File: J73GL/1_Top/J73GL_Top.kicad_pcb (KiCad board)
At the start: 2 copper layers, 315.8 x 99.2 mm, 90 parts, among them J10 Conn_01x01, J11 Conn_01x01, J12 Conn_01x01, J13 Conn_01x01, J14 Conn_01x01, J15 Conn_01x01, J16 Conn_01x01, J17 Conn_01x01, J2 Conn_01x01, J3 Conn_01x01, J4 Conn_01x01, J5 Conn_01x01, J6 Conn_01x01, J7 Conn_01x01, J8 Conn_01x01, J9 Conn_01x01, SW1 SW_PUSH, SW2 KEY_SWITCH, SW3 SW_PUSH, SW4 KEY_SWITCH, SW4 SW_PUSH, SW5 SW_PUSH, SW7 SW_PUSH, SW8 SW_PUSH

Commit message: 色々更新
・J74GLからJ73GLに変更
・色々進捗
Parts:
- removed the SW8 at (295.3, 85.7)
- SW4: footprint kbd:SW_Hole_2u -> kbd:SW_Hole_2.25u
- SW8: footprint kbd:SW_Hole -> kbd:SW_Hole_1.75
- moved SW8 11.9 mm to (288.1, 85.7)
- moved SW8 4.76 mm to (223.8, 85.7)
- moved SW8 4.76 mm to (185.7, 85.7)
- moved SW8 4.76 mm to (128.6, 85.7)
- moved SW8 4.76 mm to (90.5, 85.7)
- moved SW8 4.76 mm to (71.4, 85.7)
- moved SW8 4.76 mm to (242.9, 85.7)
- moved SW8 4.76 mm to (261.9, 85.7)
- moved SW8 4.76 mm to (204.8, 85.7)
- moved SW8 4.76 mm to (147.6, 85.7)
- moved SW8 4.76 mm to (166.7, 85.7)
- moved SW8 4.76 mm to (109.5, 85.7)
- moved SW4 2.38 mm to (40.5, 85.7)

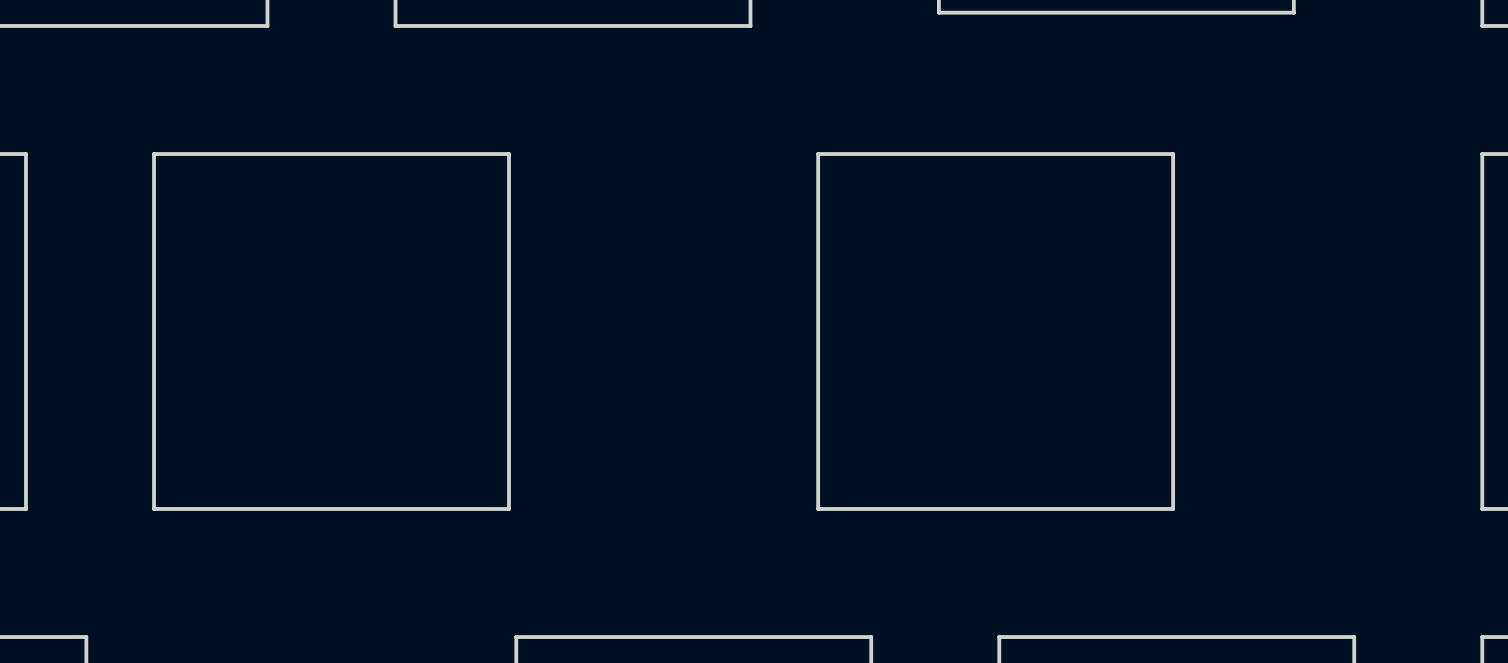
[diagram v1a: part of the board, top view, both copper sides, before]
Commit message: トッププレートのスイッチ穴を修正
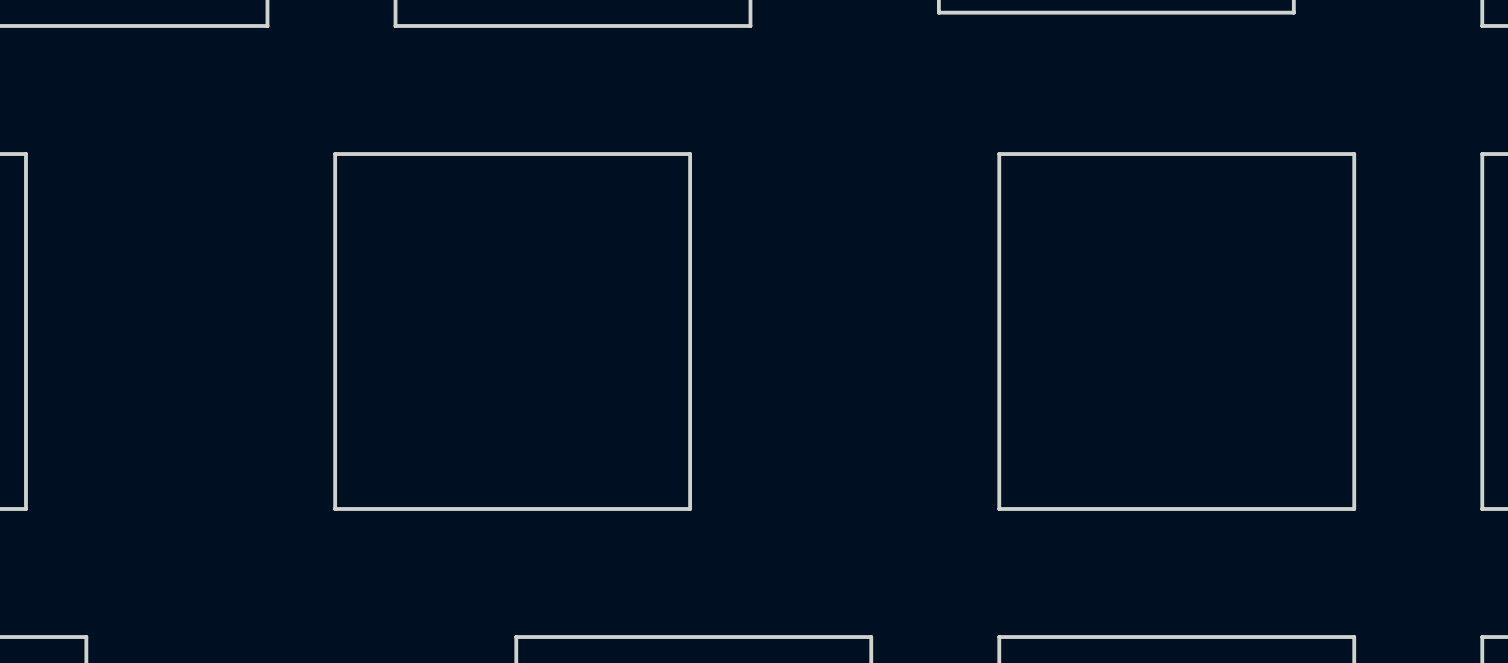
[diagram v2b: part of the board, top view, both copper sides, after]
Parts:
- moved SW8 33.3 mm to (295.3, 85.7)
- moved SW8 19.1 mm to (269.1, 85.7)
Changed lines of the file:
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@@
   )
   (module kbd:SW_Hole_1.75 (layer F.Cu)
-    (at 288.13125 85.725)
+    (at 269.08125 85.725)
     (fp_text reference SW8 (at 7 8.1) (layer F.SilkS) hide
       (effects (font (size 1 1) (thickness 0.15)))
@@
   )
   (module kbd:SW_Hole (layer F.Cu)
-    (at 261.9375 85.725)
-    (fp_text reference SW8 (at 7 8.1) (layer F.SilkS) hide
-      (effects (font (size 1 1) (thickness 0.15)))
+    (at 295.275 85.725)
+    (fp_text reference SW8 (at 7 8.1) (layer F.SilkS) hide
+      (effects (font (size 1 1) (thickness 0.15)))
